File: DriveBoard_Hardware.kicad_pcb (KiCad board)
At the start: 2 copper layers, 124.5 x 121.7 mm, 52 parts, among them SW1 SW_DPDT_x2, U1 MAX_3232, U10 Left Back, U11 TM4C129E_Launchpad_Full, U12 IRF7821PbF, U13 IRF7821PbF, U14 IRF7821PbF, U15 Strip_1, U16 Strip_2, U17 Servo_1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

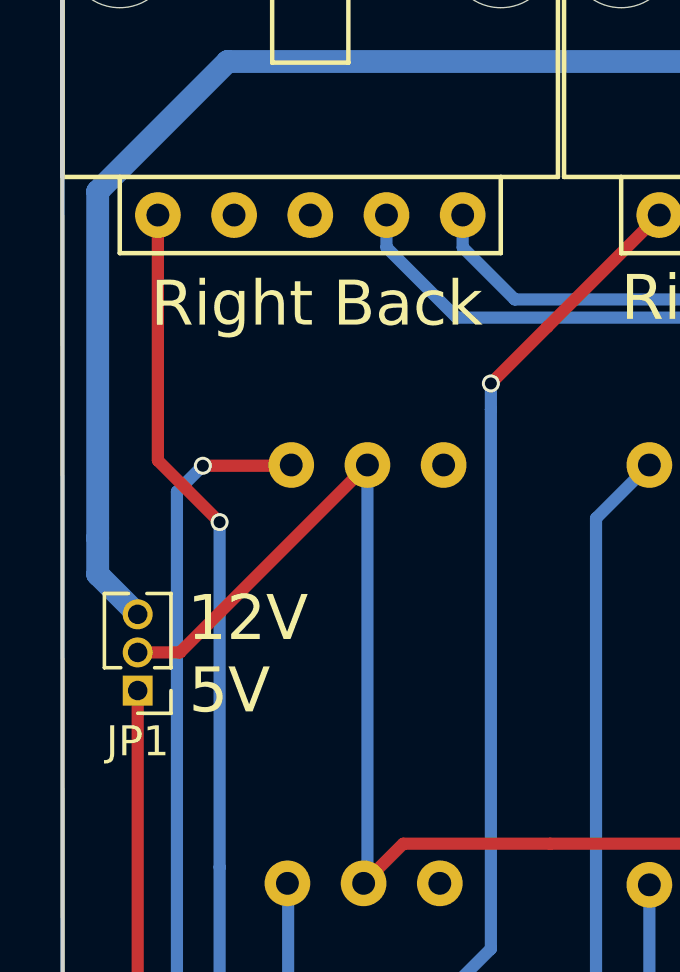
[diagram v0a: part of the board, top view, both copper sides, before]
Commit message: changed header footprint from 1.27mm to 2.54mm
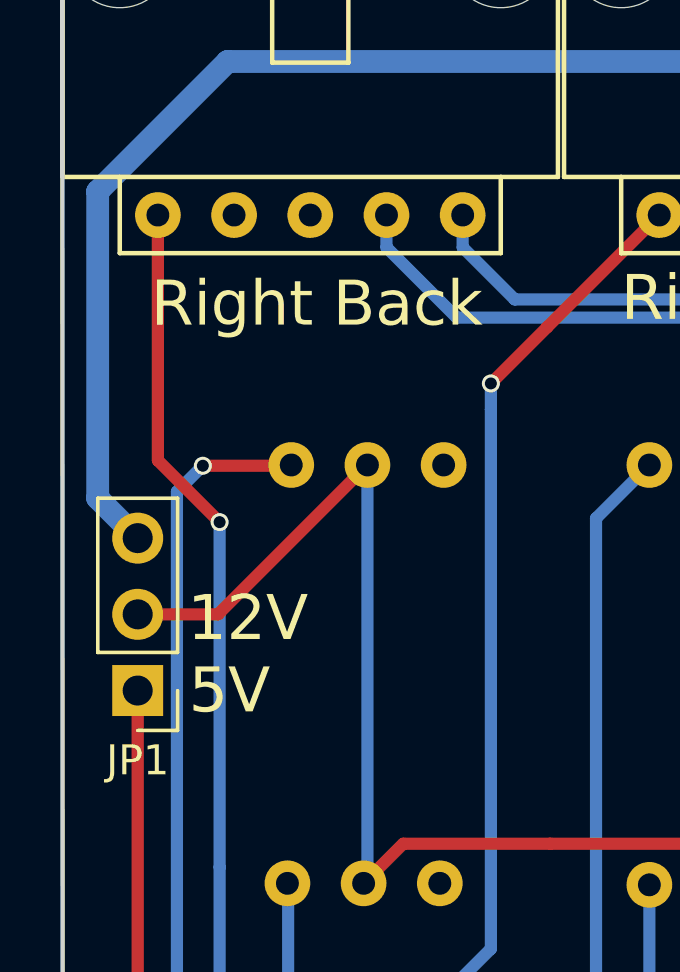
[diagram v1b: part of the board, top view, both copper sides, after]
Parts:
- JP1: footprint Pin_Headers:Pin_Header_Straight_1x03_Pitch1.27mm -> Pin_Headers:Pin_Header_Straight_1x03_Pitch2.54mm
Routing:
- net +12V: track 243.6 -> 241.0 mm
- net Net-(JP1-Pad2): track 51.4 -> 50.9 mm
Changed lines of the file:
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@@
   (general
     (links 160)
-    (no_connects 4)
-    (area 133.617899 33.706999 258.292377 155.561101)
+    (no_connects 6)
+    (area 129.864642 33.481599 258.466001 156.1536)
     (thickness 1.6)
     (drawings 41)
-    (tracks 661)
+    (tracks 660)
     (zones 0)
     (modules 52)
@@
   )
   (setup
-    (last_trace_width 0.25)
+    (last_trace_width 0.4064)
     (user_trace_width 0.254)
     (user_trace_width 0.4064)
@@
       (xy 1.623322 -1.54873) (xy 1.63531 -1.550051) (xy 1.656309 -1.543439)) (layer F.SilkS) (width 0.01))
   )
-  (module Pin_Headers:Pin_Header_Straight_1x03_Pitch1.27mm (layer F.Cu)
+  (module Pin_Headers:Pin_Header_Straight_1x03_Pitch2.54mm (layer F.Cu)
     (at 136.2075 62.865 180)
-    (descr "Through hole straight pin header, 1x03, 1.27mm pitch, single row")
-    (tags "Through hole pin header THT 1x03 1.27mm single row")
-    (fp_text reference JP1 (at 0 -1.695 180) (layer F.SilkS)
-      (effects (font (size 1 1) (thickness 0.15)))
-    )
-    (fp_text value Jumper_NC_Dual (at 0 4.235 180) (layer F.Fab)
-      (effects (font (size 1 1) (thickness 0.15)))
-    )
-    (fp_line (start -0.525 -0.635) (end 1.05 -0.635) (layer F.Fab) (width 0.1))
-    (fp_line (start 1.05 -0.635) (end 1.05 3.175) (layer F.Fab) (width 0.1))
-    (fp_line (start 1.05 3.175) (end -1.05 3.175) (layer F.Fab) (width 0.1))
-    (fp_line (start -1.05 3.175) (end -1.05 -0.11) (layer F.Fab) (width 0.1))
-    (fp_line (start -1.05 -0.11) (end -0.525 -0.635) (layer F.Fab) (width 0.1))
-    (fp_line (start -1.11 3.235) (end -0.30753 3.235) (layer F.SilkS) (width 0.12))
-    (fp_line (start 0.30753 3.235) (end 1.11 3.235) (layer F.SilkS) (width 0.12))
-    (fp_line (start -1.11 0.76) (end -1.11 3.235) (layer F.SilkS) (width 0.12))
-    (fp_line (start 1.11 0.76) (end 1.11 3.235) (layer F.SilkS) (width 0.12))
-    (fp_line (start -1.11 0.76) (end -0.563471 0.76) (layer F.SilkS) (width 0.12))
-    (fp_line (start 0.563471 0.76) (end 1.11 0.76) (layer F.SilkS) (width 0.12))
-    (fp_line (start -1.11 0) (end -1.11 -0.76) (layer F.SilkS) (width 0.12))
-    (fp_line (start -1.11 -0.76) (end 0 -0.76) (layer F.SilkS) (width 0.12))
-    (fp_line (start -1.55 -1.15) (end -1.55 3.7) (layer F.CrtYd) (width 0.05))
-    (fp_line (start -1.55 3.7) (end 1.55 3.7) (layer F.CrtYd) (width 0.05))
-    (fp_line (start 1.55 3.7) (end 1.55 -1.15) (layer F.CrtYd) (width 0.05))
-    (fp_line (start 1.55 -1.15) (end -1.55 -1.15) (layer F.CrtYd) (width 0.05))
-    (fp_text user %R (at 0 1.27 270) (layer F.Fab)
+    (descr "Through hole straight pin header, 1x03, 2.54mm pitch, single row")
+    (tags "Through hole pin header THT 1x03 2.54mm single row")
+    (fp_text reference JP1 (at 0 -2.33 180) (layer F.SilkS)
+      (effects (font (size 1 1) (thickness 0.15)))
+    )
+    (fp_text value Jumper_NC_Dual (at 0 7.41 180) (layer F.Fab)
+      (effects (font (size 1 1) (thickness 0.15)))
+    )
+    (fp_line (start -0.635 -1.27) (end 1.27 -1.27) (layer F.Fab) (width 0.1))
+    (fp_line (start 1.27 -1.27) (end 1.27 6.35) (layer F.Fab) (width 0.1))
+    (fp_line (start 1.27 6.35) (end -1.27 6.35) (layer F.Fab) (width 0.1))
+    (fp_line (start -1.27 6.35) (end -1.27 -0.635) (layer F.Fab) (width 0.1))
+    (fp_line (start -1.27 -0.635) (end -0.635 -1.27) (layer F.Fab) (width 0.1))
+    (fp_line (start -1.33 6.41) (end 1.33 6.41) (layer F.SilkS) (width 0.12))
+    (fp_line (start -1.33 1.27) (end -1.33 6.41) (layer F.SilkS) (width 0.12))
+    (fp_line (start 1.33 1.27) (end 1.33 6.41) (layer F.SilkS) (width 0.12))
+    (fp_line (start -1.33 1.27) (end 1.33 1.27) (layer F.SilkS) (width 0.12))
+    (fp_line (start -1.33 0) (end -1.33 -1.33) (layer F.SilkS) (width 0.12))
+    (fp_line (start -1.33 -1.33) (end 0 -1.33) (layer F.SilkS) (width 0.12))
+    (fp_line (start -1.8 -1.8) (end -1.8 6.85) (layer F.CrtYd) (width 0.05))
+    (fp_line (start -1.8 6.85) (end 1.8 6.85) (layer F.CrtYd) (width 0.05))
+    (fp_line (start 1.8 6.85) (end 1.8 -1.8) (layer F.CrtYd) (width 0.05))
+    (fp_line (start 1.8 -1.8) (end -1.8 -1.8) (layer F.CrtYd) (width 0.05))
+    (fp_text user %R (at 0 2.54 270) (layer F.Fab)
       (effects (font (size 1 1) (thickness 0.15)))
     )
-    (pad 1 thru_hole rect (at 0 0 180) (size 1 1) (drill 0.65) (layers *.Cu *.Mask)
+    (pad 1 thru_hole rect (at 0 0 180) (size 1.7 1.7) (drill 1) (layers *.Cu *.Mask)
       (net 18 +5V))
-    (pad 2 thru_hole oval (at 0 1.27 180) (size 1 1) (drill 0.65) (layers *.Cu *.Mask)
+    (pad 2 thru_hole oval (at 0 2.54 180) (size 1.7 1.7) (drill 1) (layers *.Cu *.Mask)
       (net 84 "Net-(JP1-Pad2)"))
-    (pad 3 thru_hole oval (at 0 2.54 180) (size 1 1) (drill 0.65) (layers *.Cu *.Mask)
+    (pad 3 thru_hole oval (at 0 5.08 180) (size 1.7 1.7) (drill 1) (layers *.Cu *.Mask)
       (net 14 +12V))
-    (model ${KISYS3DMOD}/Pin_Headers.3dshapes/Pin_Header_Straight_1x03_Pitch1.27mm.wrl
+    (model ${KISYS3DMOD}/Pin_Headers.3dshapes/Pin_Header_Straight_1x03_Pitch2.54mm.wrl
       (at (xyz 0 0 0))
       (scale (xyz 1 1 1))
@@
   (segment (start 161.3408 92.7404) (end 161.3408 91.4654) (width 0.254) (layer F.Cu) (net 13))
   (via (at 161.3408 91.4654) (size 0.6) (drill 0.4) (layers F.Cu B.Cu) (net 13))
-  (segment (start 134.874 57.785) (end 134.874 58.9915) (width 0.762) (layer B.Cu) (net 14))
+  (segment (start 134.874 46.228) (end 134.874 56.4515) (width 0.762) (layer B.Cu) (net 14))
+  (segment (start 134.874 56.4515) (end 136.2075 57.785) (width 0.762) (layer B.Cu) (net 14))
   (segment (start 139.2047 41.8973) (end 134.874 46.228) (width 0.762) (layer B.Cu) (net 14))
-  (segment (start 134.874 46.228) (end 134.874 57.785) (width 0.762) (layer B.Cu) (net 14))
   (segment (start 248.7041 41.8973) (end 139.2047 41.8973) (width 0.762) (layer B.Cu) (net 14))
-  (segment (start 134.874 58.9915) (end 136.2075 60.325) (width 0.762) (layer B.Cu) (net 14))
   (segment (start 249.1232 60.6044) (end 249.1232 83.6168) (width 0.762) (layer B.Cu) (net 14))
   (segment (start 249.1232 83.6168) (end 249.1232 91.6442) (width 0.762) (layer B.Cu) (net 14))
@@
   (segment (start 208.9658 118.6434) (end 206.817 118.6434) (width 0.4064) (layer F.Cu) (net 83))
   (segment (start 206.817 118.6434) (end 206.2734 119.187) (width 0.4064) (layer F.Cu) (net 83))
+  (segment (start 136.2075 60.325) (end 138.8872 60.325) (width 0.4064) (layer F.Cu) (net 84))
+  (segment (start 138.8872 60.325) (end 143.8656 55.3466) (width 0.4064) (layer F.Cu) (net 84))
   (segment (start 149.9616 67.9704) (end 145.0594 67.9704) (width 0.4064) (layer F.Cu) (net 84))
   (segment (start 154.432 67.9704) (end 149.9616 67.9704) (width 0.4064) (layer F.Cu) (net 84))
   (segment (start 145.0594 67.9704) (end 143.7386 69.2912) (width 0.4064) (layer F.Cu) (net 84))
-  (segment (start 136.2075 61.595) (end 137.6172 61.595) (width 0.4064) (layer F.Cu) (net 84))
-  (segment (start 137.6172 61.595) (end 143.8656 55.3466) (width 0.4064) (layer F.Cu) (net 84))
   (segment (start 155.8036 69.342) (end 154.432 67.9704) (width 0.4064) (layer F.Cu) (net 84))
   (segment (start 155.8036 55.3466) (end 155.8036 56.42423) (width 0.4064) (layer B.Cu) (net 84))
